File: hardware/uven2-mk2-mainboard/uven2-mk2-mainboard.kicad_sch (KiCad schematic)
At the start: 103 parts, among them J1 LEDs, J10 GND, J11 24V, J12 GND, J13 24V, J14 GND, J15 Chamber_Control, J16 USB_A, J17 PowerON/OFF, J2 1-282834-0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

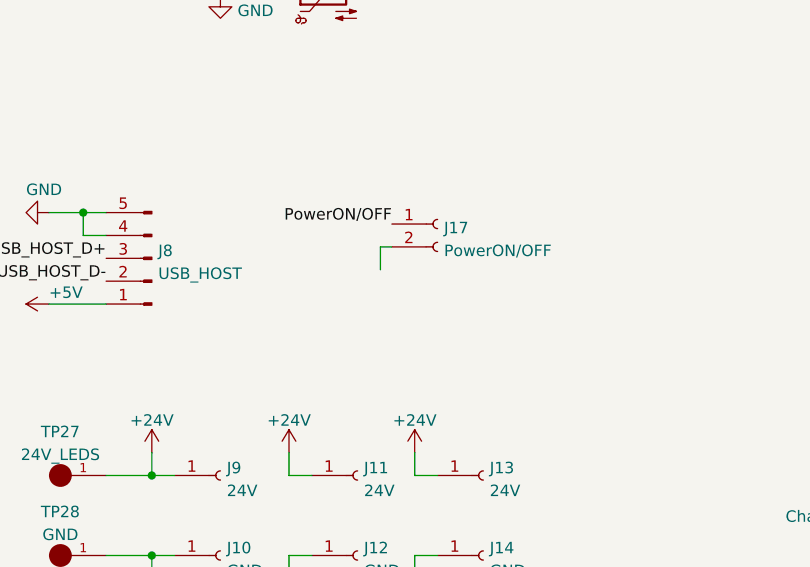
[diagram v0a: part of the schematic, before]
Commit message: uven pocket layout almost finished
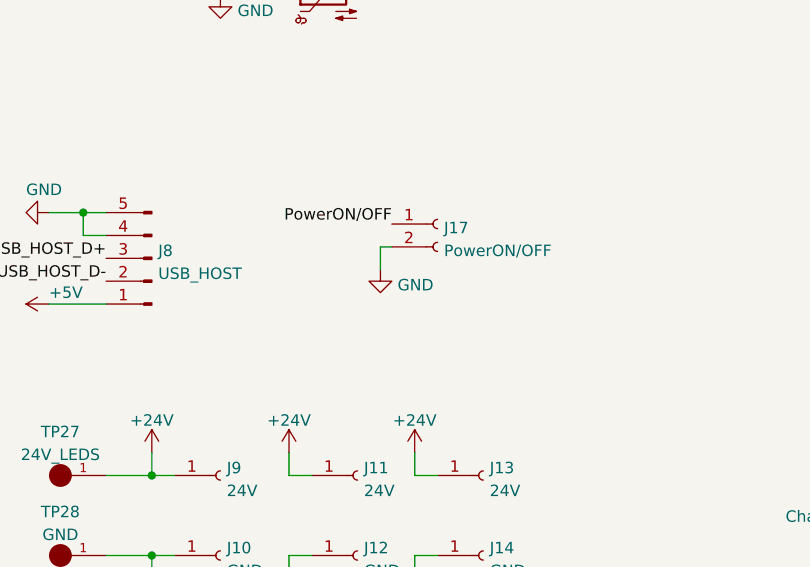
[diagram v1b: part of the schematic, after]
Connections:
- net GND: now also J17.2 (Pin_2)
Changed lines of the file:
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@@
     (pin "1")
   )
+  (symbol (lib_id "power:GND") (at 156.21 185.42 0) (unit 1)
+    (in_bom yes) (on_board yes) (fields_autoplaced)
+    (property "Reference" "#PWR?" (id 0) (at 156.21 191.77 0)
+      (effects (font (size 1.27 1.27)) hide)
+    )
+    (property "Value" "GND" (id 1) (at 158.115 187.1238 0)
+      (effects (font (size 1.27 1.27)) (justify left))
+    )
+    (property "Footprint" "" (id 2) (at 156.21 185.42 0)
+      (effects (font (size 1.27 1.27)) hide)
+    )
+    (property "Datasheet" "" (id 3) (at 156.21 185.42 0)
+      (effects (font (size 1.27 1.27)) hide)
+    )
+    (pin "1")
+  )
   (symbol (lib_id "power:GND") (at 248.92 223.52 90) (unit 1)
     (in_bom yes) (on_board yes)
@@
       (reference "#PWR0261") (unit 1) (value "GND") (footprint "")
     )
+    (path "/151f91d9-889f-4f71-9f4b-b8fa4c237dbf"
+      (reference "#PWR?") (unit 1) (value "GND") (footprint "")
+    )
     (path "/8f15e43a-f43b-4fe7-a252-39f2b26b193d"

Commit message: ordered on jlcpcb
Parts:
- added FID1, FID2, FID3: Fiducial, Fiducial:Fiducial_1mm_Dia_2.54mm_Outer_CopperTop, symbol Mechanical:Fiducial
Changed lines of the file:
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@@
     (pin "1")
   )
+  (symbol (lib_id "Mechanical:Fiducial") (at 165.1 258.445 0) (unit 1)
+    (in_bom yes) (on_board yes) (fields_autoplaced)
+    (property "Reference" "FID1" (id 0) (at 167.259 257.6103 0)
+      (effects (font (size 1.27 1.27)) (justify left))
+    )
+    (property "Value" "Fiducial" (id 1) (at 167.259 260.1472 0)
+      (effects (font (size 1.27 1.27)) (justify left))
+    )
+    (property "Footprint" "Fiducial:Fiducial_1mm_Dia_2.54mm_Outer_CopperTop" (id 2) (at 165.1 258.445 0)
+      (effects (font (size 1.27 1.27)) hide)
+    )
+    (property "Datasheet" "~" (id 3) (at 165.1 258.445 0)
+      (effects (font (size 1.27 1.27)) hide)
+    )
+  )
   (symbol (lib_id "power:GND") (at 248.92 233.68 90) (unit 1)
     (in_bom yes) (on_board yes)
@@
   (symbol (lib_id "power:GND") (at 156.21 185.42 0) (unit 1)
     (in_bom yes) (on_board yes) (fields_autoplaced)
-    (property "Reference" "#PWR?" (id 0) (at 156.21 191.77 0)
+    (property "Reference" "#PWR0234" (id 0) (at 156.21 191.77 0)
       (effects (font (size 1.27 1.27)) hide)
     )
@@
     (pin "1")
   )
+  (symbol (lib_id "Mechanical:Fiducial") (at 165.1 265.43 0) (unit 1)
+    (in_bom yes) (on_board yes) (fields_autoplaced)
+    (property "Reference" "FID2" (id 0) (at 167.259 264.5953 0)
+      (effects (font (size 1.27 1.27)) (justify left))
+    )
+    (property "Value" "Fiducial" (id 1) (at 167.259 267.1322 0)
+      (effects (font (size 1.27 1.27)) (justify left))
+    )
+    (property "Footprint" "Fiducial:Fiducial_1mm_Dia_2.54mm_Outer_CopperTop" (id 2) (at 165.1 265.43 0)
+      (effects (font (size 1.27 1.27)) hide)
+    )
+    (property "Datasheet" "~" (id 3) (at 165.1 265.43 0)
+      (effects (font (size 1.27 1.27)) hide)
+    )
+  )
   (symbol (lib_id "power:+3.3V") (at 55.88 171.45 270) (unit 1)
     (in_bom yes) (on_board yes) (fields_autoplaced)
-    (property "Reference" "#PWR?" (id 0) (at 52.07 171.45 0)
+    (property "Reference" "#PWR0233" (id 0) (at 52.07 171.45 0)
       (effects (font (size 1.27 1.27)) hide)
     )
@@
     (pin "2")
   )
+  (symbol (lib_id "Mechanical:Fiducial") (at 165.1 273.05 0) (unit 1)
+    (in_bom yes) (on_board yes) (fields_autoplaced)
+    (property "Reference" "FID3" (id 0) (at 167.259 272.2153 0)
+      (effects (font (size 1.27 1.27)) (justify left))
+    )
+    (property "Value" "Fiducial" (id 1) (at 167.259 274.7522 0)
+      (effects (font (size 1.27 1.27)) (justify left))
+    )
+    (property "Footprint" "Fiducial:Fiducial_1mm_Dia_2.54mm_Outer_CopperTop" (id 2) (at 165.1 273.05 0)
+      (effects (font (size 1.27 1.27)) hide)
+    )
+    (property "Datasheet" "~" (id 3) (at 165.1 273.05 0)
+      (effects (font (size 1.27 1.27)) hide)
+    )
+  )
   (symbol (lib_id "RCWCTE:RCWCTE") (at 153.67 116.84 0) (unit 1)
     (in_bom yes) (on_board yes)
@@
       (reference "#PWR0232") (unit 1) (value "GND") (footprint "")
     )
+    (path "/8f15e43a-f43b-4fe7-a252-39f2b26b193d"
+      (reference "#PWR0233") (unit 1) (value "+3.3V") (footprint "")
+    )
+    (path "/151f91d9-889f-4f71-9f4b-b8fa4c237dbf"
+      (reference "#PWR0234") (unit 1) (value "GND") (footprint "")
+    )
     (path "/4c42a249-1580-449a-b7c9-aacbced8ee3d"
       (reference "#PWR0235") (unit 1) (value "GND") (footprint "")
@@
       (reference "#PWR0261") (unit 1) (value "GND") (footprint "")
     )
-    (path "/151f91d9-889f-4f71-9f4b-b8fa4c237dbf"
-      (reference "#PWR?") (unit 1) (value "GND") (footprint "")
-    )
-    (path "/8f15e43a-f43b-4fe7-a252-39f2b26b193d"
-      (reference "#PWR?") (unit 1) (value "+3.3V") (footprint "")
-    )
     (path "/74394a4e-e68c-4574-bde0-dd3ca18d2b15"
       (reference "C1") (unit 1) (value "100n") (footprint "Capacitor_SMD:C_0603_1608Metric_Pad1.08x0.95mm_HandSolder")
@@
       (reference "C40") (unit 1) (value "100n") (footprint "Capacitor_SMD:C_0603_1608Metric_Pad1.08x0.95mm_HandSolder")
     )
+    (path "/0b0897a0-dd79-4f91-b5e1-17984eab9cee"
+      (reference "FID1") (unit 1) (value "Fiducial") (footprint "Fiducial:Fiducial_1mm_Dia_2.54mm_Outer_CopperTop")
+    )
+    (path "/8df5fd72-c77d-423c-bb25-8af3749b025e"
+      (reference "FID2") (unit 1) (value "Fiducial") (footprint "Fiducial:Fiducial_1mm_Dia_2.54mm_Outer_CopperTop")
+    )
+    (path "/d4ce0402-0549-42f5-86c9-433404365837"
+      (reference "FID3") (unit 1) (value "Fiducial") (footprint "Fiducial:Fiducial_1mm_Dia_2.54mm_Outer_CopperTop")
+    )
     (path "/fd53414d-fed1-4192-a4a6-6e71719f5ee3"

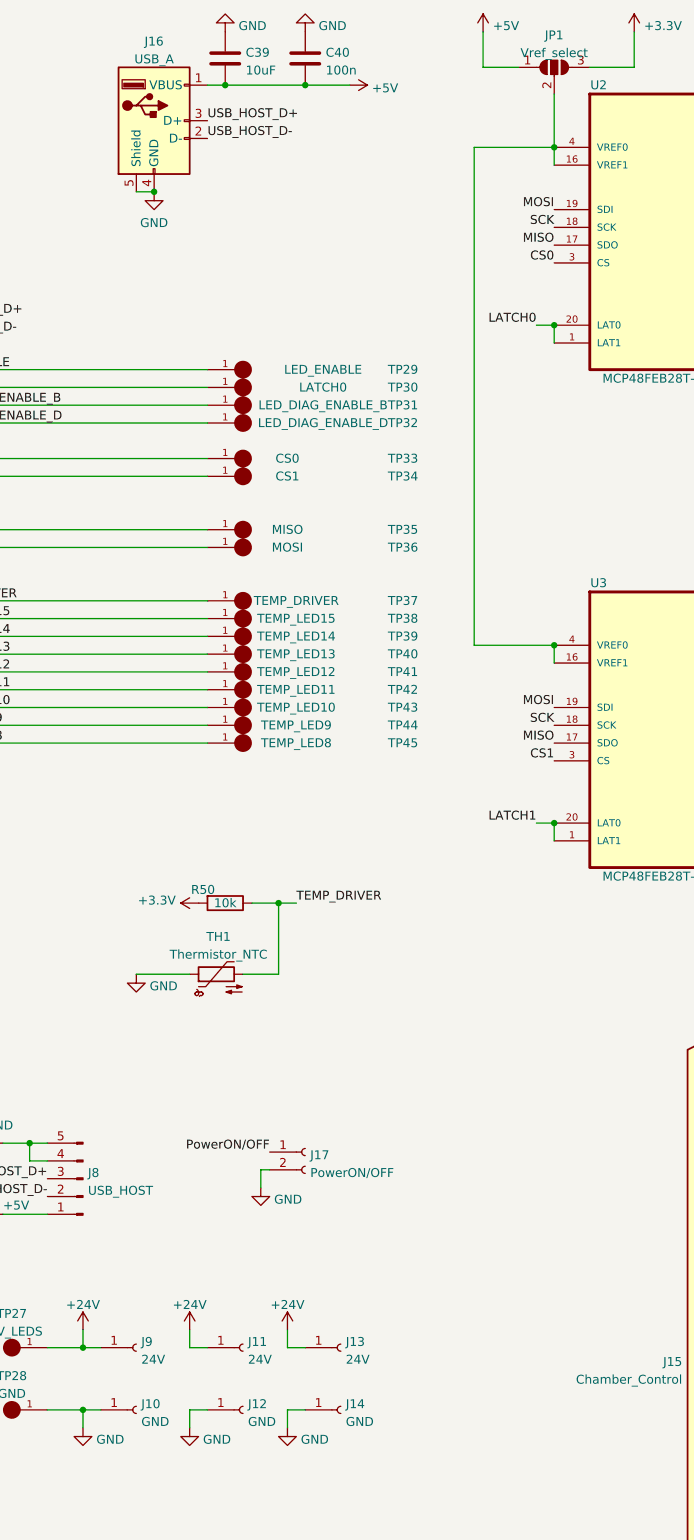
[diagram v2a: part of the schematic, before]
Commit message: fixed 3.3V trace missing, added footage
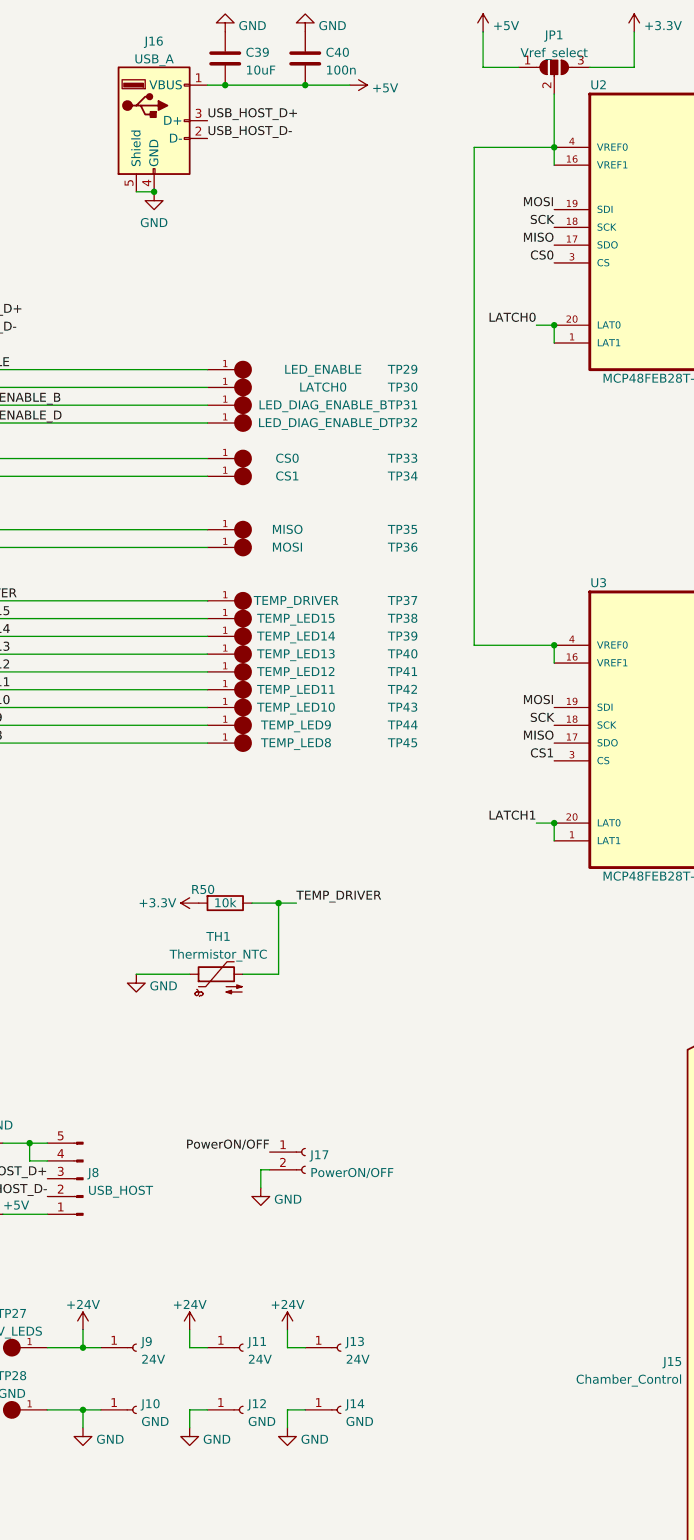
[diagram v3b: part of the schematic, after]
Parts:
- U2, U3: symbol MCP48FEB28T-20E_ST:MCP48FEB28T-20E/ST -> MCP48FEB28T-20E_ST:MCP48FEB28T-20E/ST
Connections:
- net +3V3 is gone; now on net +3.3V: R50.2
